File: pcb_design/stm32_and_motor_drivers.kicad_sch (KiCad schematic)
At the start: 51 parts, among them J9 Conn_01x06_Pin, U11 STM32G431KBU6, U12 DRV8256PRGER, U13 DRV8256PRGER, U14 DRV8256PRGER, U15 DRV8256PRGER

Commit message: fix: Update BOM export configuration
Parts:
- TP10, TP14, TP15, TP16, TP17, TP9: now left out of the parts list
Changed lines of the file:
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@@
 		(body_style 1)
 		(exclude_from_sim no)
-		(in_bom yes)
+		(in_bom no)
 		(on_board yes)
 		(in_pos_files yes)
@@
 		(body_style 1)
 		(exclude_from_sim no)
-		(in_bom yes)
+		(in_bom no)
 		(on_board yes)
 		(in_pos_files yes)
@@
 		(body_style 1)
 		(exclude_from_sim no)
-		(in_bom yes)
+		(in_bom no)
 		(on_board yes)
 		(in_pos_files yes)
@@
 		(body_style 1)
 		(exclude_from_sim no)
-		(in_bom yes)
+		(in_bom no)
 		(on_board yes)
 		(in_pos_files yes)
@@
 		(body_style 1)
 		(exclude_from_sim no)
-		(in_bom yes)
+		(in_bom no)
 		(on_board yes)
 		(in_pos_files yes)
@@
 		(body_style 1)
 		(exclude_from_sim no)
-		(in_bom yes)
+		(in_bom no)
 		(on_board yes)
 		(in_pos_files yes)

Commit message: fix(PCB): Update MPN and footprint for some passives
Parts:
- C42, C43, C45, C46, C51, C52, C57, C58: footprint Capacitor_SMD:C_0603_1608Metric -> Capacitor_SMD:C_0805_2012Metric
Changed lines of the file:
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@@
 			)
 		)
-		(property "Footprint" "Capacitor_SMD:C_0603_1608Metric"
+		(property "Footprint" "Capacitor_SMD:C_0805_2012Metric"
 			(at 73.3552 139.7 0)
 			(hide yes)
@@
 			)
 		)
-		(property "Footprint" "Capacitor_SMD:C_0603_1608Metric"
+		(property "Footprint" "Capacitor_SMD:C_0805_2012Metric"
 			(at 172.4152 137.16 0)
 			(hide yes)
@@
 			)
 		)
-		(property "Footprint" "Capacitor_SMD:C_0603_1608Metric"
+		(property "Footprint" "Capacitor_SMD:C_0805_2012Metric"
 			(at 181.3052 82.55 0)
 			(hide yes)
@@
 			)
 		)
-		(property "Footprint" "Capacitor_SMD:C_0603_1608Metric"
+		(property "Footprint" "Capacitor_SMD:C_0805_2012Metric"
 			(at 112.7252 49.53 0)
 			(hide yes)
@@
 			)
 		)
-		(property "Footprint" "Capacitor_SMD:C_0603_1608Metric"
+		(property "Footprint" "Capacitor_SMD:C_0805_2012Metric"
 			(at 181.3052 137.16 0)
 			(hide yes)
@@
 			)
 		)
-		(property "Footprint" "Capacitor_SMD:C_0603_1608Metric"
+		(property "Footprint" "Capacitor_SMD:C_0805_2012Metric"
 			(at 64.4652 139.7 0)
 			(hide yes)
@@
 			)
 		)
-		(property "Footprint" "Capacitor_SMD:C_0603_1608Metric"
+		(property "Footprint" "Capacitor_SMD:C_0805_2012Metric"
 			(at 172.4152 82.55 0)
 			(hide yes)
@@
 			)
 		)
-		(property "Footprint" "Capacitor_SMD:C_0603_1608Metric"
+		(property "Footprint" "Capacitor_SMD:C_0805_2012Metric"
 			(at 103.8352 49.53 0)
 			(hide yes)

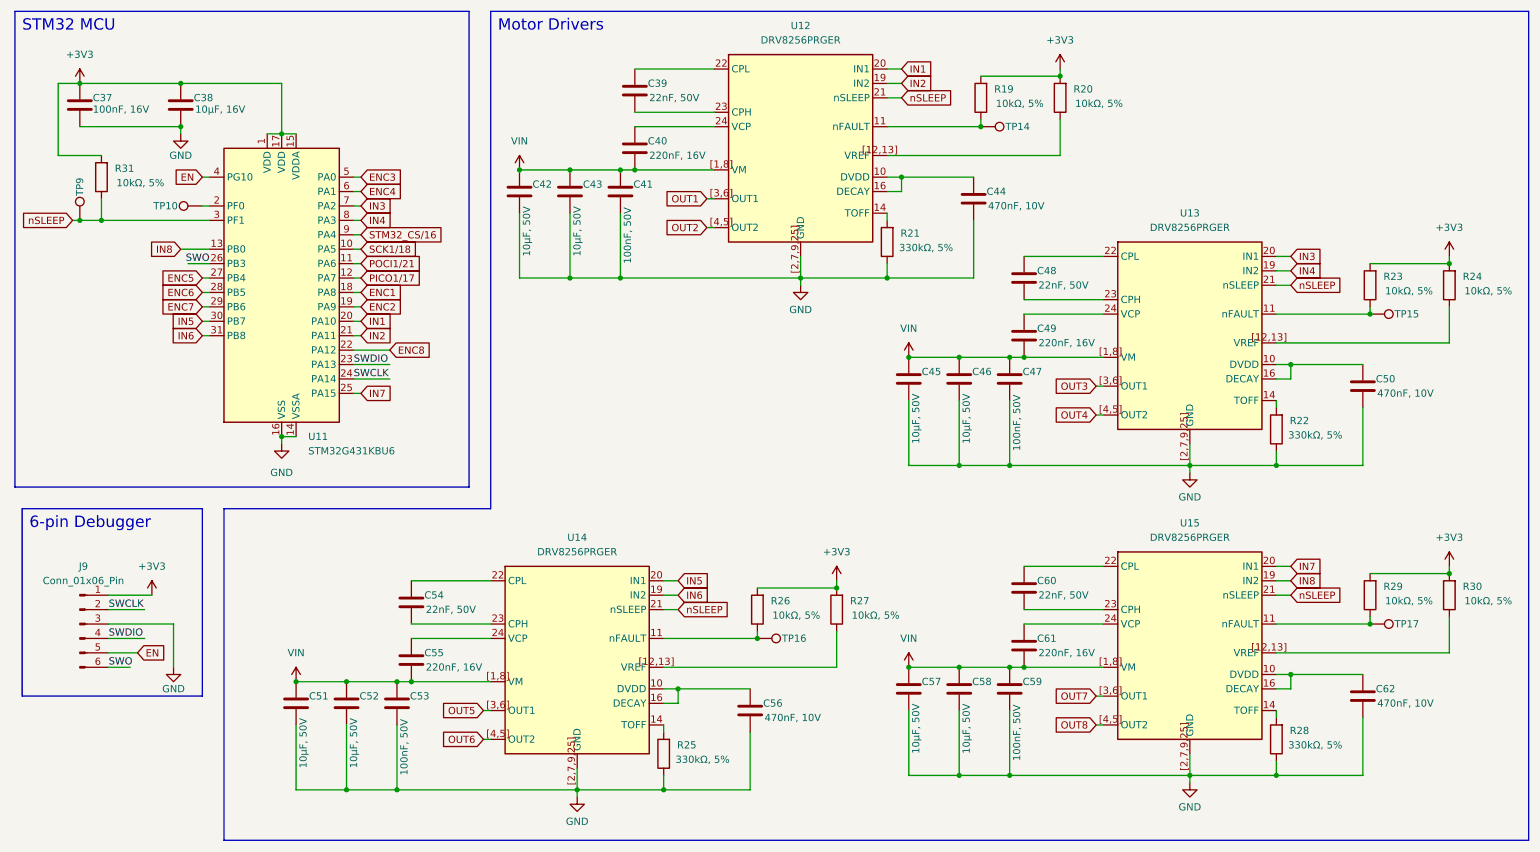
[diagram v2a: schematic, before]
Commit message: feat(pcb): Add more test points
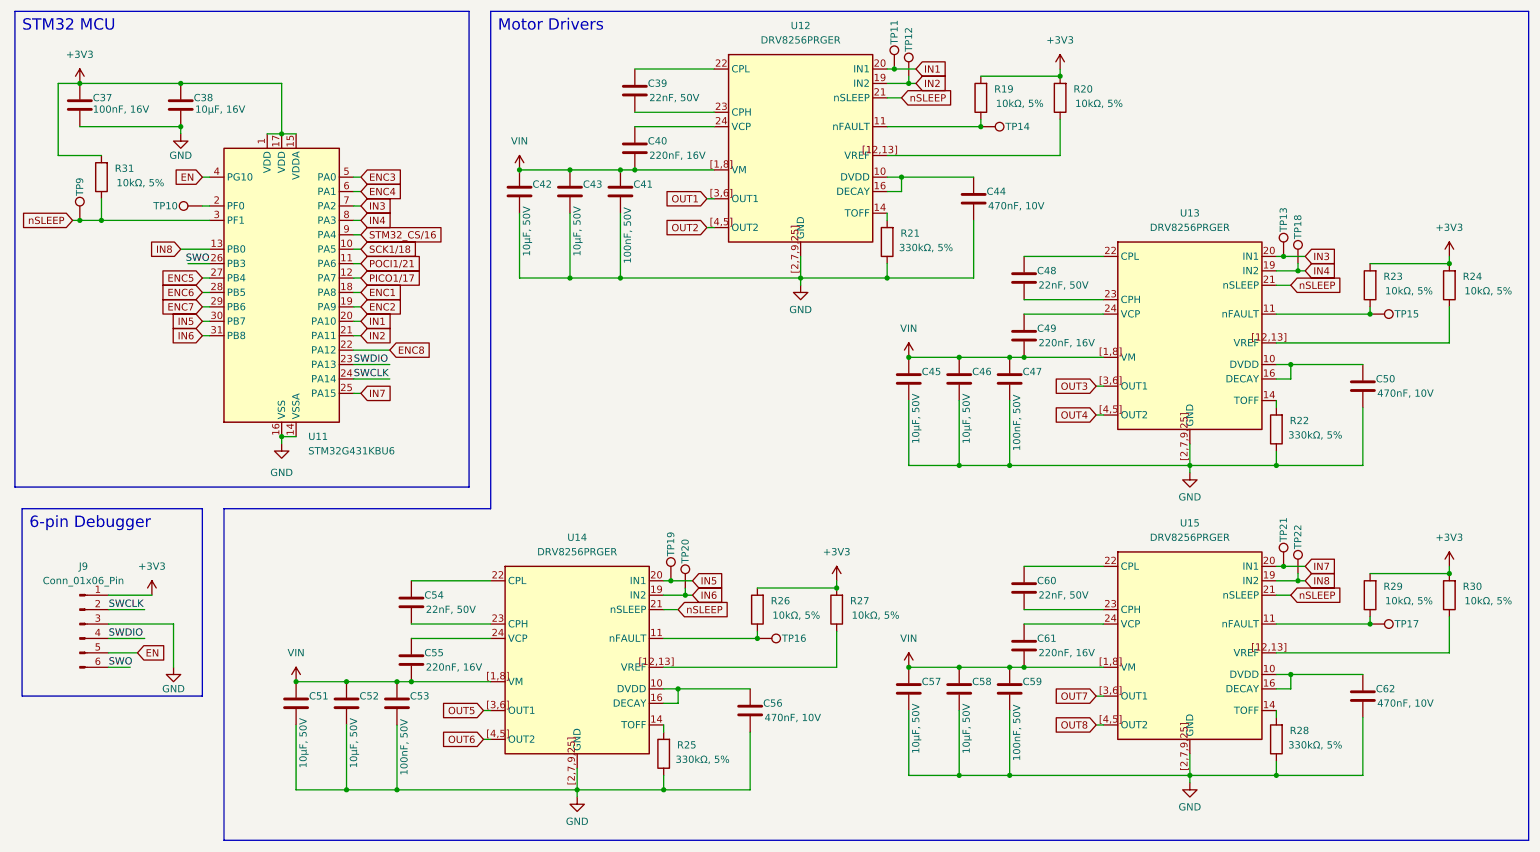
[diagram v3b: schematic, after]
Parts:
- added TP11, TP12, TP13, TP18, TP19, TP20, TP21, TP22: TestPoint, TestPoint:TestPoint_Pad_D1.0mm, symbol Connector:TestPoint
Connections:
- net IN1: now also TP11.1
- net IN2: now also TP12.1
- net IN3: now also TP13.1
- net IN4: now also TP18.1
- net IN5: now also TP19.1
- net IN6: now also TP20.1
- net IN7: now also TP21.1
- net IN8: now also TP22.1
